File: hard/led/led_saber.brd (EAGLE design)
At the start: 100 x 80 mm, 5 parts, among them IC2 CAT4101

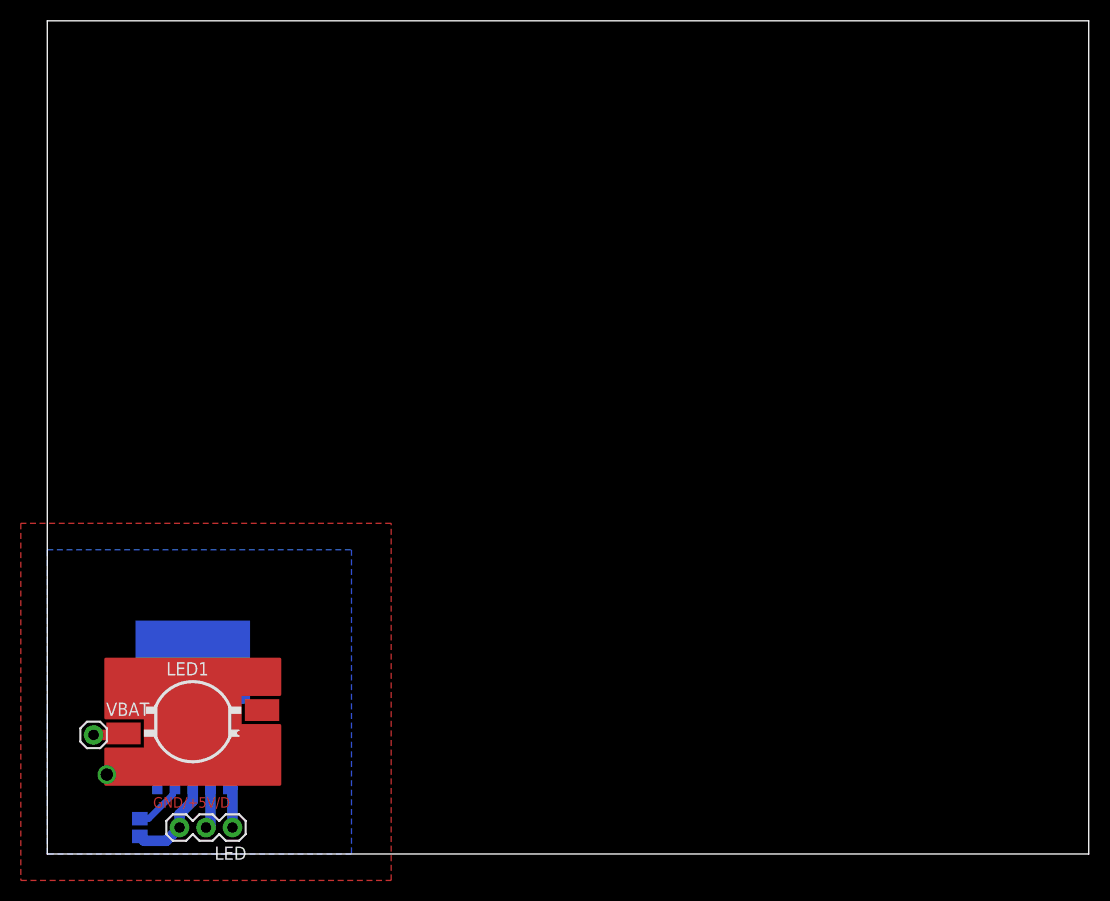
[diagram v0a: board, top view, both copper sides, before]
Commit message: Carte led puissance terminée
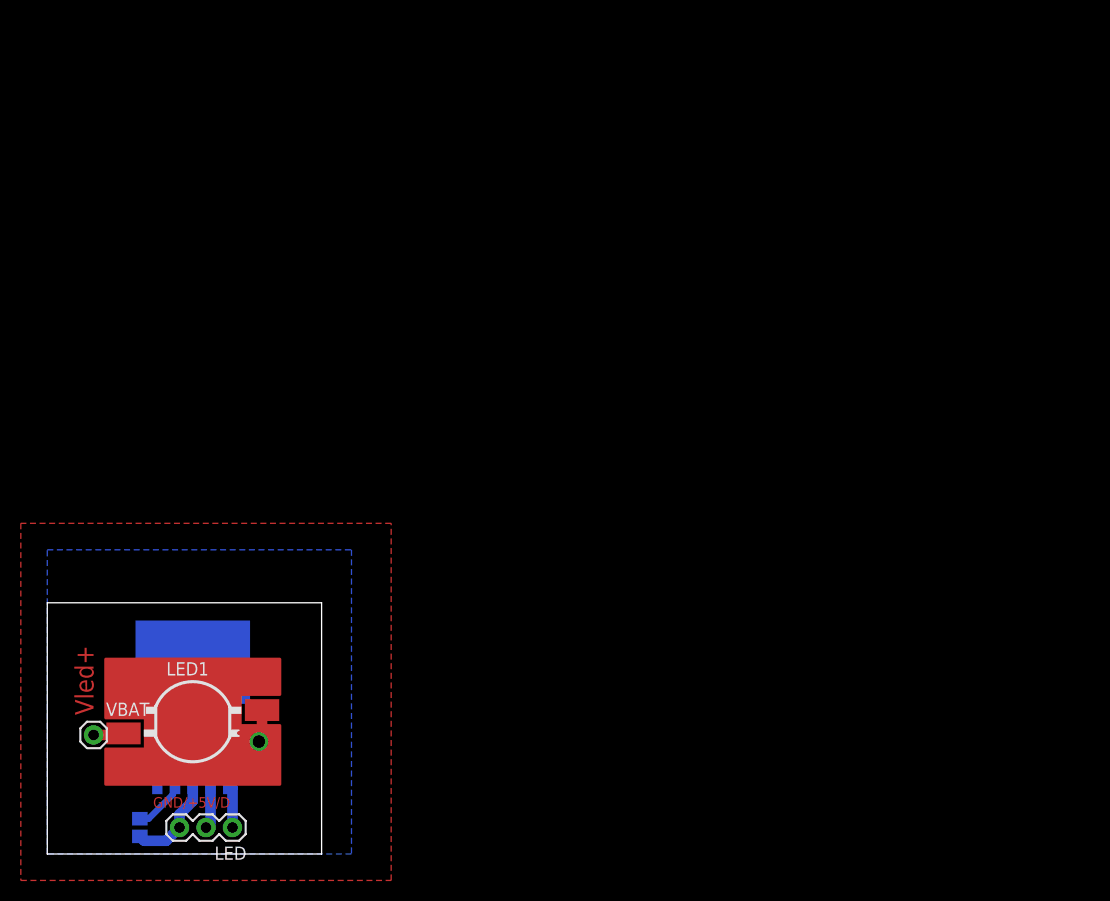
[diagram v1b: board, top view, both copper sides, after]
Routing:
- net N$1: track 5.91 -> 16.8 mm, vias 0 -> 1
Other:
- board size 100 x 80 mm -> 26.3 x 24.1 mm
- board text added: "Vled+"
